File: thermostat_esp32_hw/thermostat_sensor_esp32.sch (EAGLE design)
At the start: 52 parts, among them IC2 ESP32-WROOM-32UE-N16, J1 TB-5.08-P-2P_BL, J2 TB-5.08-P-2P_BL, J3 TB-5.08-P-2P_BL, K1 G5LE-1_5VDC, K2 G5LE-1_5VDC, Q1 TLP185_SE_T, Q2 TLP185_SE_T

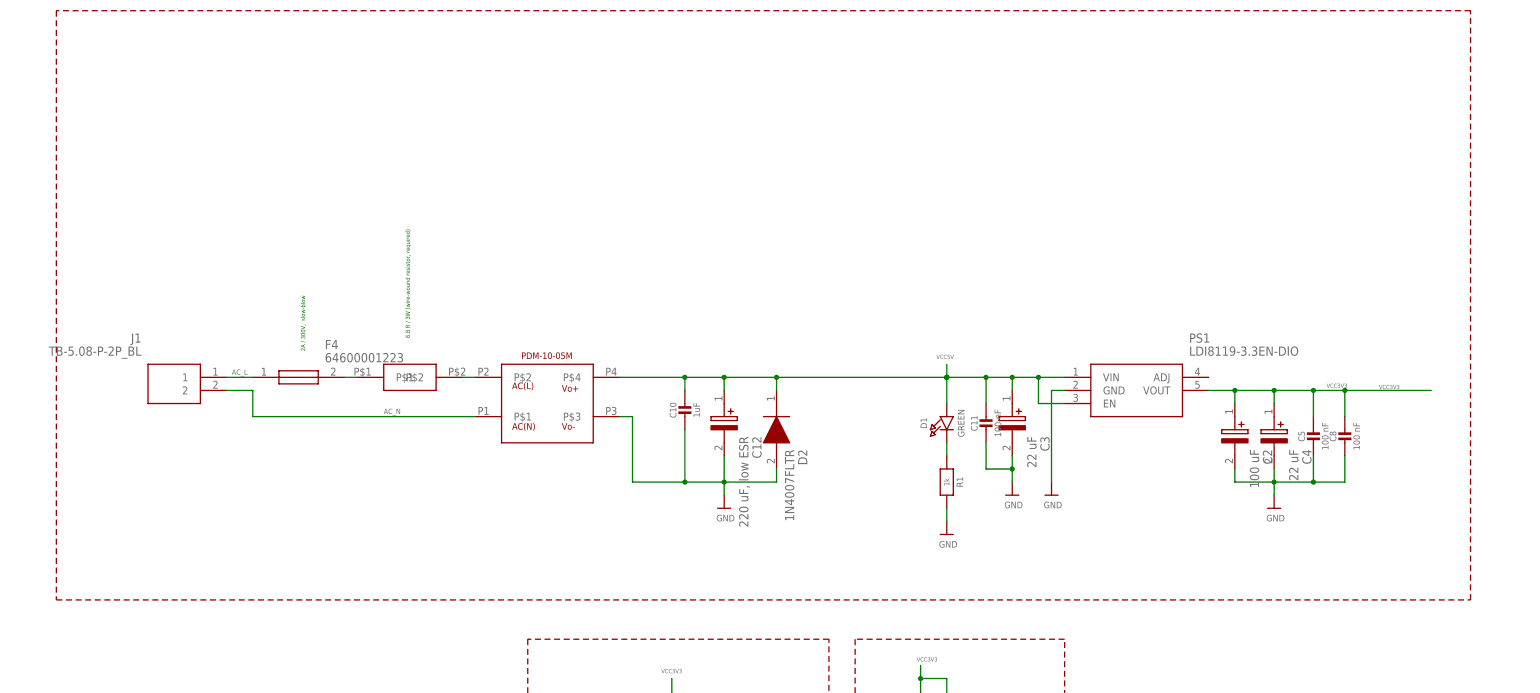
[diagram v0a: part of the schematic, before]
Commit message: different voltage regulator
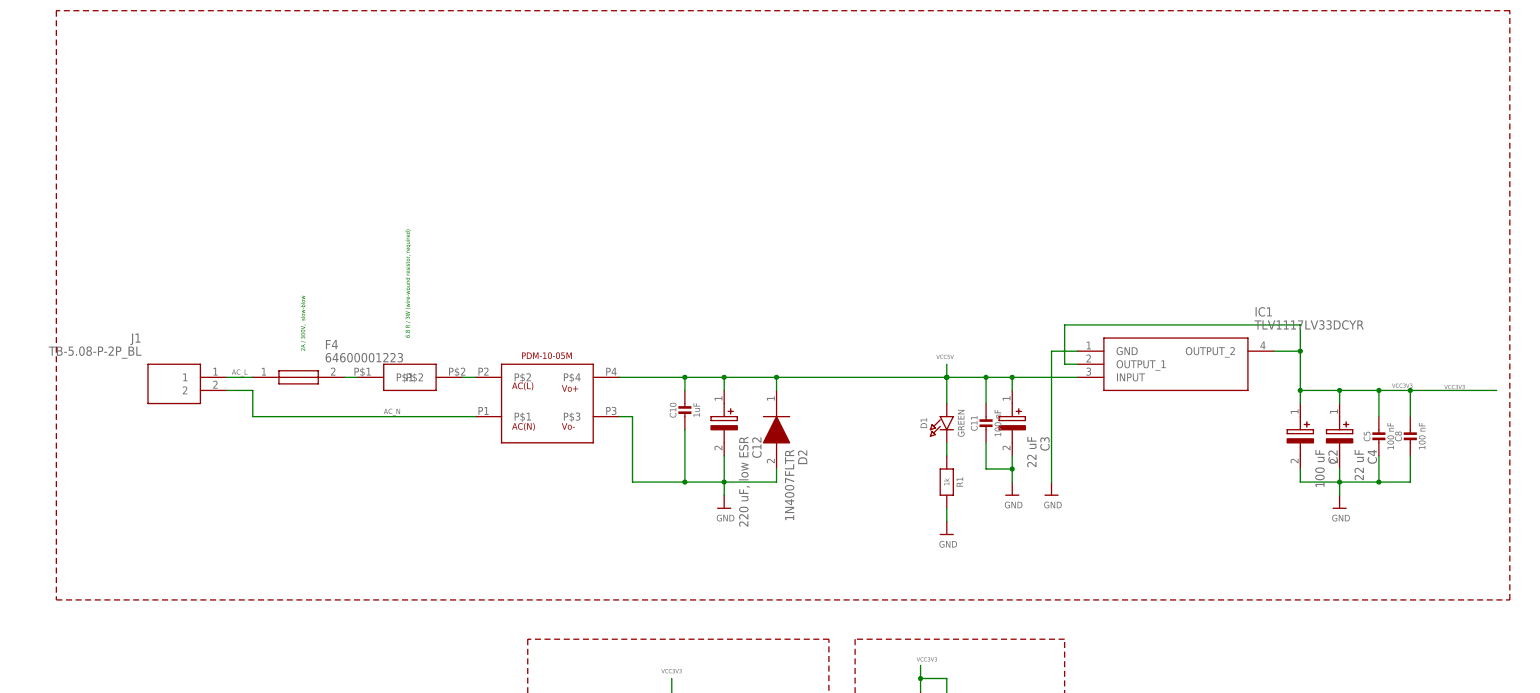
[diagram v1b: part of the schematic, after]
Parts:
- removed PS1: LDI8119-3.3EN-DIO, AP2202K-3.3TRG1:AP2202K-3.3TRG1
- added IC1: TLV1117LV33DCYR, TLV1117LV33DCYR:TLV1117LV33DCYR
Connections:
- net GND: now also IC1.GND; no longer PS1.GND
- net VCC3V3: now also IC1.OUTPUT_1, IC1.OUTPUT_2; no longer PS1.VOUT
- net VCC5V: now also IC1.INPUT; no longer PS1.EN, PS1.VIN
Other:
- moved on the sheet: C2, C4, C5, C8
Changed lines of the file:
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@@
 <part name="R5" library="microbuilder" deviceset="RESISTOR" device="_0603" value="10k"/>
 <part name="U$7" library="microbuilder" deviceset="GND" device=""/>
-<part name="PS1" library="AP2202K-3.3TRG1" deviceset="AP2202K-3.3TRG1" device="" value="LDI8119-3.3EN-DIO"/>
 <part name="C4" library="293D226X9010A2TE3" deviceset="293D226X9010A2TE3" device="" value="22 uF">
 <attribute name="DESCRIPTION" value="Solid Tantalum Surface Mount Chip Capacitors TANTAMOUNT(TM), Molded Case, Standard Industrial Grade"/>
@@
 <part name="C12" library="EEUFR1E221B" deviceset="EEUFR1E221B" device="" value="220 uF, low ESR"/>
 <part name="SV3" library="con-lstb" deviceset="MA05-1" device=""/>
+<part name="IC1" library="TLV1117LV33DCYR" deviceset="TLV1117LV33DCYR" device=""/>
 </parts>
 <sheets>
@@
 <wire x1="304.8" y1="83.82" x2="111.76" y2="83.82" width="0.1524" layer="94" style="shortdash"/>
 <wire x1="20.32" y1="383.54" x2="20.32" y2="269.24" width="0.1524" layer="94" style="shortdash"/>
-<wire x1="20.32" y1="269.24" x2="294.64" y2="269.24" width="0.1524" layer="94" style="shortdash"/>
-<wire x1="294.64" y1="269.24" x2="294.64" y2="383.54" width="0.1524" layer="94" style="shortdash"/>
-<wire x1="294.64" y1="383.54" x2="20.32" y2="383.54" width="0.1524" layer="94" style="shortdash"/>
+<wire x1="20.32" y1="269.24" x2="302.26" y2="269.24" width="0.1524" layer="94" style="shortdash"/>
+<wire x1="302.26" y1="269.24" x2="302.26" y2="383.54" width="0.1524" layer="94" style="shortdash"/>
+<wire x1="302.26" y1="383.54" x2="20.32" y2="383.54" width="0.1524" layer="94" style="shortdash"/>
 <wire x1="175.26" y1="213.36" x2="175.26" y2="162.56" width="0.1524" layer="94" style="shortdash"/>
 <wire x1="175.26" y1="162.56" x2="215.9" y2="162.56" width="0.1524" layer="94" style="shortdash"/>
@@
 <instance part="U$6" gate="G$1" x="193.04" y="281.94"/>
 <instance part="U$10" gate="G$1" x="149.86" y="287.02"/>
-<instance part="C2" gate="G$1" x="248.92" y="307.34" rot="R270"/>
+<instance part="C2" gate="G$1" x="261.62" y="307.34" rot="R270"/>
 <instance part="SV1" gate="G$1" x="162.56" y="223.52" rot="R180"/>
 <instance part="R4" gate="G$1" x="139.7" y="241.3" rot="R90"/>
 <instance part="R5" gate="G$1" x="134.62" y="241.3" rot="R90"/>
 <instance part="U$7" gate="G$1" x="152.4" y="210.82"/>
-<instance part="PS1" gate="G$1" x="215.9" y="312.42"/>
-<instance part="C4" gate="G$1" x="256.54" y="307.34" rot="R270"/>
+<instance part="C4" gate="G$1" x="269.24" y="307.34" rot="R270"/>
 <instance part="U$5" gate="G$1" x="213.36" y="289.56"/>
-<instance part="U$8" gate="G$1" x="256.54" y="287.02"/>
+<instance part="U$8" gate="G$1" x="269.24" y="287.02"/>
 <instance part="SV2" gate="G$1" x="208.28" y="190.5" rot="R180"/>
 <instance part="U$12" gate="G$1" x="198.12" y="172.72"/>
@@
 <instance part="U$13" gate="G$1" x="132.08" y="177.8"/>
 <instance part="R8" gate="G$1" x="142.24" y="185.42" rot="R90"/>
-<instance part="C8" gate="G$1" x="270.256" y="299.72"/>
+<instance part="C8" gate="G$1" x="282.956" y="299.72"/>
 <instance part="IC2" gate="G$1" x="30.48" y="116.84"/>
 <instance part="U$16" gate="G$1" x="20.32" y="81.28" rot="R270"/>
@@
 <instance part="U$18" gate="G$1" x="71.12" y="55.88"/>
 <instance part="C11" gate="G$1" x="200.66" y="302.26"/>
-<instance part="C5" gate="G$1" x="264.16" y="299.72"/>
+<instance part="C5" gate="G$1" x="276.86" y="299.72"/>
 <instance part="R1" gate="G$1" x="193.04" y="292.1" rot="R270"/>
 <instance part="C3" gate="G$1" x="205.74" y="309.88" rot="R270"/>
@@
 <instance part="C12" gate="G$1" x="149.86" y="309.88" rot="R270"/>
 <instance part="SV3" gate="G$1" x="162.56" y="180.34" rot="R180"/>
+<instance part="IC1" gate="G$1" x="218.44" y="317.5"/>
 </instances>
 <busses>
@@
 <wire x1="200.66" y1="312.42" x2="205.74" y2="312.42" width="0.1524" layer="91"/>
 <wire x1="205.74" y1="312.42" x2="205.74" y2="309.88" width="0.1524" layer="91"/>
-<pinref part="PS1" gate="G$1" pin="VIN"/>
-<wire x1="205.74" y1="312.42" x2="210.82" y2="312.42" width="0.1524" layer="91"/>
 <junction x="205.74" y="312.42"/>
-<pinref part="PS1" gate="G$1" pin="EN"/>
-<wire x1="210.82" y1="312.42" x2="215.9" y2="312.42" width="0.1524" layer="91"/>
-<wire x1="215.9" y1="307.34" x2="210.82" y2="307.34" width="0.1524" layer="91"/>
-<wire x1="210.82" y1="307.34" x2="210.82" y2="312.42" width="0.1524" layer="91"/>
-<junction x="210.82" y="312.42"/>
+<wire x1="205.74" y1="312.42" x2="218.44" y2="312.42" width="0.1524" layer="91"/>
 <pinref part="C11" gate="G$1" pin="1"/>
 <wire x1="200.66" y1="307.34" x2="200.66" y2="312.42" width="0.1524" layer="91"/>
@@
 <label x="191.008" y="315.976" size="0.8128" layer="95"/>
 <pinref part="C12" gate="G$1" pin="+"/>
+<pinref part="IC1" gate="G$1" pin="INPUT"/>
 </segment>
 <segment>
@@
 </segment>
 <segment>
-<pinref part="PS1" gate="G$1" pin="GND"/>
 <pinref part="U$5" gate="G$1" pin="GND"/>
-<wire x1="215.9" y1="309.88" x2="213.36" y2="309.88" width="0.1524" layer="91"/>
-<wire x1="213.36" y1="309.88" x2="213.36" y2="292.1" width="0.1524" layer="91"/>
+<wire x1="213.36" y1="317.5" x2="213.36" y2="292.1" width="0.1524" layer="91"/>
+<pinref part="IC1" gate="G$1" pin="GND"/>
+<wire x1="213.36" y1="317.5" x2="218.44" y2="317.5" width="0.1524" layer="91"/>
 </segment>
 <segment>
 <pinref part="U$8" gate="G$1" pin="GND"/>
 <pinref part="C4" gate="G$1" pin="-"/>
-<wire x1="256.54" y1="294.64" x2="256.54" y2="292.1" width="0.1524" layer="91"/>
-<wire x1="256.54" y1="292.1" x2="256.54" y2="289.56" width="0.1524" layer="91"/>
-<wire x1="264.16" y1="297.18" x2="264.16" y2="292.1" width="0.1524" layer="91"/>
-<wire x1="264.16" y1="292.1" x2="256.54" y2="292.1" width="0.1524" layer="91"/>
-<junction x="256.54" y="292.1"/>
+<wire x1="269.24" y1="294.64" x2="269.24" y2="292.1" width="0.1524" layer="91"/>
+<wire x1="269.24" y1="292.1" x2="269.24" y2="289.56" width="0.1524" layer="91"/>
+<wire x1="276.86" y1="297.18" x2="276.86" y2="292.1" width="0.1524" layer="91"/>
+<wire x1="276.86" y1="292.1" x2="269.24" y2="292.1" width="0.1524" layer="91"/>
+<junction x="269.24" y="292.1"/>
 <pinref part="C8" gate="G$1" pin="2"/>
-<wire x1="264.16" y1="292.1" x2="270.256" y2="292.1" width="0.1524" layer="91"/>
-<wire x1="270.256" y1="292.1" x2="270.256" y2="297.18" width="0.1524" layer="91"/>
-<junction x="264.16" y="292.1"/>
+<wire x1="276.86" y1="292.1" x2="282.956" y2="292.1" width="0.1524" layer="91"/>
+<wire x1="282.956" y1="292.1" x2="282.956" y2="297.18" width="0.1524" layer="91"/>
+<junction x="276.86" y="292.1"/>
 <pinref part="C2" gate="G$1" pin="-"/>
-<wire x1="248.92" y1="294.64" x2="248.92" y2="292.1" width="0.1524" layer="91"/>
-<wire x1="248.92" y1="292.1" x2="256.54" y2="292.1" width="0.1524" layer="91"/>
+<wire x1="261.62" y1="294.64" x2="261.62" y2="292.1" width="0.1524" layer="91"/>
+<wire x1="261.62" y1="292.1" x2="269.24" y2="292.1" width="0.1524" layer="91"/>
 <pinref part="C5" gate="G$1" pin="2"/>
 </segment>
@@
 <net name="VCC3V3" class="0">
 <segment>
-<pinref part="PS1" gate="G$1" pin="VOUT"/>
 <pinref part="C4" gate="G$1" pin="+"/>
-<wire x1="243.84" y1="309.88" x2="248.92" y2="309.88" width="0.1524" layer="91"/>
-<wire x1="248.92" y1="309.88" x2="256.54" y2="309.88" width="0.1524" layer="91"/>
-<wire x1="256.54" y1="309.88" x2="256.54" y2="307.34" width="0.1524" layer="91"/>
-<wire x1="256.54" y1="309.88" x2="264.16" y2="309.88" width="0.1524" layer="91"/>
-<junction x="256.54" y="309.88"/>
-<label x="266.7" y="310.388" size="0.8128" layer="95"/>
-<label x="276.86" y="310.134" size="0.8128" layer="95"/>
-<wire x1="264.16" y1="309.88" x2="270.256" y2="309.88" width="0.1524" layer="91"/>
-<wire x1="270.256" y1="309.88" x2="287.02" y2="309.88" width="0.1524" layer="91"/>
-<wire x1="264.16" y1="304.8" x2="264.16" y2="309.88" width="0.1524" layer="91"/>
-<junction x="264.16" y="309.88"/>
+<wire x1="261.62" y1="309.88" x2="269.24" y2="309.88" width="0.1524" layer="91"/>
+<wire x1="269.24" y1="309.88" x2="269.24" y2="307.34" width="0.1524" layer="91"/>
+<wire x1="269.24" y1="309.88" x2="276.86" y2="309.88" width="0.1524" layer="91"/>
+<junction x="269.24" y="309.88"/>
+<label x="279.4" y="310.388" size="0.8128" layer="95"/>
+<label x="289.56" y="310.134" size="0.8128" layer="95"/>
+<wire x1="276.86" y1="309.88" x2="282.956" y2="309.88" width="0.1524" layer="91"/>
+<wire x1="282.956" y1="309.88" x2="299.72" y2="309.88" width="0.1524" layer="91"/>
+<wire x1="276.86" y1="304.8" x2="276.86" y2="309.88" width="0.1524" layer="91"/>
+<junction x="276.86" y="309.88"/>
 <pinref part="C8" gate="G$1" pin="1"/>
-<wire x1="270.256" y1="304.8" x2="270.256" y2="309.88" width="0.1524" layer="91"/>
-<junction x="270.256" y="309.88"/>
+<wire x1="282.956" y1="304.8" x2="282.956" y2="309.88" width="0.1524" layer="91"/>
+<junction x="282.956" y="309.88"/>
 <pinref part="C2" gate="G$1" pin="+"/>
-<wire x1="248.92" y1="307.34" x2="248.92" y2="309.88" width="0.1524" layer="91"/>
-<junction x="248.92" y="309.88"/>
+<wire x1="261.62" y1="307.34" x2="261.62" y2="309.88" width="0.1524" layer="91"/>
+<junction x="261.62" y="309.88"/>
 <pinref part="C5" gate="G$1" pin="1"/>
-</segment>
-<segment>
+<pinref part="IC1" gate="G$1" pin="OUTPUT_1"/>
+<wire x1="218.44" y1="314.96" x2="215.9" y2="314.96" width="0.1524" layer="91"/>
+<wire x1="215.9" y1="314.96" x2="215.9" y2="322.58" width="0.1524" layer="91"/>
+<wire x1="215.9" y1="322.58" x2="261.62" y2="322.58" width="0.1524" layer="91"/>
+<wire x1="261.62" y1="322.58" x2="261.62" y2="317.5" width="0.1524" layer="91"/>
+<pinref part="IC1" gate="G$1" pin="OUTPUT_2"/>
+<wire x1="261.62" y1="317.5" x2="256.54" y2="317.5" width="0.1524" layer="91"/>
+<wire x1="261.62" y1="317.5" x2="261.62" y2="309.88" width="0.1524" layer="91"/>
+<junction x="261.62" y="317.5"/>
+</segment>
+<segment>

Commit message: minor pcb adjustments
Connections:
- net CLK: now also IC2.IO18; no longer IC2.IO21
- net DQ2: now also IC2.IO21; no longer IC2.IO18
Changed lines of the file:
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@@
 </segment>
 <segment>
-<pinref part="IC2" gate="G$1" pin="IO21"/>
-<wire x1="68.58" y1="96.52" x2="76.2" y2="96.52" width="0.1524" layer="91"/>
-<label x="71.374" y="96.774" size="0.8128" layer="95"/>
+<pinref part="IC2" gate="G$1" pin="IO18"/>
+<wire x1="68.58" y1="104.14" x2="76.2" y2="104.14" width="0.1524" layer="91"/>
+<label x="71.628" y="104.394" size="0.8128" layer="95" font="vector"/>
 </segment>
 </net>
@@
 <net name="DQ2" class="0">
 <segment>
-<pinref part="IC2" gate="G$1" pin="IO18"/>
-<wire x1="68.58" y1="104.14" x2="76.2" y2="104.14" width="0.1524" layer="91"/>
-<label x="71.628" y="104.394" size="0.8128" layer="95" font="vector"/>
-</segment>
-<segment>
 <pinref part="SV2" gate="G$1" pin="2"/>
 <wire x1="200.66" y1="190.5" x2="187.96" y2="190.5" width="0.1524" layer="91"/>
@@
 <junction x="187.96" y="190.5"/>
 </segment>
+<segment>
+<pinref part="IC2" gate="G$1" pin="IO21"/>
+<wire x1="68.58" y1="96.52" x2="76.2" y2="96.52" width="0.1524" layer="91"/>
+<label x="71.374" y="96.774" size="0.8128" layer="95"/>
+</segment>
 </net>

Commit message: fixes to fw and hw of thermostat
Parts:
- R11, R16: value 120 R -> 0 R
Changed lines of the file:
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@@
 <part name="U$3" library="microbuilder" deviceset="GND" device=""/>
 <part name="U$9" library="microbuilder" deviceset="GND" device=""/>
-<part name="R11" library="microbuilder" deviceset="RESISTOR" device="_0603" value="120 R"/>
+<part name="R11" library="microbuilder" deviceset="RESISTOR" device="_0603" value="0 R"/>
 <part name="J2" library="TB-5.08-P-2P_BL" deviceset="TB-5.08-P-2P_BL" device="">
 <attribute name="DESCRIPTION" value="PCB terminal block; angled 90; 5.08mm; ways: 2; on PCBs; 1.5mm2"/>
@@
 <part name="U$14" library="microbuilder" deviceset="GND" device=""/>
 <part name="U$15" library="microbuilder" deviceset="GND" device=""/>
-<part name="R16" library="microbuilder" deviceset="RESISTOR" device="_0603" value="120 R"/>
+<part name="R16" library="microbuilder" deviceset="RESISTOR" device="_0603" value="0 R"/>
 <part name="J3" library="TB-5.08-P-2P_BL" deviceset="TB-5.08-P-2P_BL" device="">
 <attribute name="DESCRIPTION" value="PCB terminal block; angled 90; 5.08mm; ways: 2; on PCBs; 1.5mm2"/>

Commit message: orp module added on thermostat base board
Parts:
- added U$21: ORP_PROBE, other:ORP_PROBE
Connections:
- net GND: now also U$21.GND
- net RELAY1: now also U$21.SDA
- net RELAY2: now also U$21.SCL
- net VCC3V3: now also U$21.VCC3V3
- net VCC5V: now also U$21.VCC5V
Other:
- note added: "ORP probe module"
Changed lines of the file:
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@@
 <part name="SV3" library="con-lstb" deviceset="MA05-1" device=""/>
 <part name="IC1" library="TLV1117LV33DCYR" deviceset="TLV1117LV33DCYR" device=""/>
+<part name="U$21" library="other" deviceset="ORP_PROBE" device=""/>
 </parts>
 <sheets>
@@
 <wire x1="170.18" y1="261.62" x2="111.76" y2="261.62" width="0.1524" layer="94" style="shortdash"/>
 <wire x1="170.18" y1="203.2" x2="111.76" y2="203.2" width="0.1524" layer="94" style="shortdash"/>
+<text x="231.14" y="248.92" size="1.778" layer="94">ORP probe module</text>
 </plain>
 <instances>
@@
 <instance part="SV3" gate="G$1" x="162.56" y="180.34" rot="R180"/>
 <instance part="IC1" gate="G$1" x="218.44" y="317.5"/>
+<instance part="U$21" gate="G$1" x="238.76" y="238.76"/>
 </instances>
 <busses>
@@
 <wire x1="193.04" y1="43.18" x2="193.04" y2="53.34" width="0.1524" layer="91"/>
 <label x="191.77" y="53.848" size="1.016" layer="95"/>
+</segment>
+<segment>
+<wire x1="256.54" y1="243.84" x2="243.84" y2="243.84" width="0.1524" layer="91"/>
+<label x="251.206" y="244.348" size="0.8128" layer="95"/>
+<pinref part="U$21" gate="G$1" pin="VCC5V"/>
 </segment>
 </net>
@@
 <wire x1="132.08" y1="182.88" x2="132.08" y2="180.34" width="0.1524" layer="91"/>
 </segment>
+<segment>
+<wire x1="256.54" y1="233.68" x2="243.84" y2="233.68" width="0.1524" layer="91"/>
+<label x="251.206" y="233.934" size="0.8128" layer="95"/>
+<pinref part="U$21" gate="G$1" pin="GND"/>
+</segment>
 </net>
 <net name="EN" class="0">
@@
 <wire x1="68.58" y1="109.22" x2="76.2" y2="109.22" width="0.1524" layer="91"/>
 <label x="71.628" y="109.474" size="0.8128" layer="95" font="vector"/>
+</segment>
+<segment>
+<wire x1="256.54" y1="238.76" x2="243.84" y2="238.76" width="0.1524" layer="91"/>
+<label x="251.206" y="239.268" size="0.8128" layer="95"/>
+<pinref part="U$21" gate="G$1" pin="SDA"/>
 </segment>
 </net>
@@
 <wire x1="68.58" y1="101.6" x2="76.2" y2="101.6" width="0.1524" layer="91"/>
 <label x="71.628" y="101.854" size="0.8128" layer="95" font="vector"/>
+</segment>
+<segment>
+<wire x1="256.54" y1="236.22" x2="243.84" y2="236.22" width="0.1524" layer="91"/>
+<label x="251.206" y="236.474" size="0.8128" layer="95"/>
+<pinref part="U$21" gate="G$1" pin="SCL"/>
 </segment>
 </net>
@@
 <label x="130.81" y="193.802" size="0.8128" layer="95" font="vector"/>
 </segment>
-</net>
+<segment>
+<wire x1="256.54" y1="241.3" x2="243.84" y2="241.3" width="0.1524" layer="91"/>
+<label x="251.206" y="241.808" size="0.8128" layer="95"/>
+<pinref part="U$21" gate="G$1" pin="VCC3V3"/>
+</segment>
+</net>
